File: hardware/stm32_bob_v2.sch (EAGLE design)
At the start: 54 parts, among them U1 F3_DISCOVERY, U2 LSF0108, U3 INA827, U4 INA827

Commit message: Added version 2 of board using 40 pin header
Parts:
- removed 5V_IO: (no value), SparkFun-Connectors:M081X08
- removed AIN1, AIN2, EXT_REF: M02PTH, SparkFun-Connectors:M02PTH
- removed JP1, JP2: M25X2, SparkFun-Connectors:M25X2
- added U$1: M40, SparkFun-Connectors:M40
- R10, R11, R12, R13, R6, R7, R8, R9: value (none) -> 1k
- R14, R15, R16, R17, R18, R19, R20, R21: value (none) -> 1.6k
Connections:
- removed net N$1: 5V_IO.1, R14.1, U2.B1
- removed net N$10: AIN1.2, U3.IN+
- removed net N$11: AIN2.2, U4.IN+
- removed net N$12: AIN2.1, U4.IN-
- removed net N$2: 5V_IO.2, R15.1, U2.B2
- removed net N$3: 5V_IO.3, R16.1, U2.B3
- removed net N$4: 5V_IO.4, R17.1, U2.B4
- removed net N$5: 5V_IO.5, R18.2, U2.B5
- removed net N$6: 5V_IO.6, R19.2, U2.B6
- removed net N$7: 5V_IO.7, R20.2, U2.B7
- removed net N$8: 5V_IO.8, R21.2, U2.B8
- removed net N$9: AIN1.1, U3.IN-
- new net AIN1_N: U$1.35, U3.IN-
- new net AIN1_P: U$1.36, U3.IN+
- new net AIN2_N: U$1.37, U4.IN-
- new net AIN2_P: U$1.38, U4.IN+
- new net PA14_5: R18.2, U$1.29, U2.B5
- new net PA15_5: R19.2, U$1.28, U2.B6
- new net PC10_5: R20.2, U$1.27, U2.B7
- new net PC11_5: R21.2, U$1.26, U2.B8
- new net PE11_5: R15.1, U$1.33, U2.B2
- new net PE13_5: R16.1, U$1.32, U2.B3
- new net PE14_5: R17.1, U$1.31, U2.B4
- new net PE9_5: R14.1, U$1.34, U2.B1
- net 3V: now also C1.1, C2.1, U$1.1, U$1.2, U3.V+, U4.V+; no longer JP1.1, JP1.2
- net 5V: now also U$1.3, U$1.4; no longer C1.1, C2.1, JP2.1, JP2.2, U3.V+, U4.V+
- net BOOT0: no longer JP2.19
- net GND: now also U$1.10, U$1.20, U$1.30, U$1.40; no longer EXT_REF.1, JP1.3, JP1.49, JP1.50, JP2.49, JP2.50
- net NRST: no longer JP1.4
- net PA0: no longer JP1.12
- net PA1: now also U$1.5; no longer JP1.9
- net PA10: no longer JP2.43
- net PA11: now also U$1.21; no longer JP2.42
- net PA12: now also U$1.22; no longer JP2.41
- net PA13: no longer JP2.40
- net PA14: no longer JP2.37
- net PA15: no longer JP2.38
- net PA2: now also U$1.6; no longer JP1.14
- net PA3: now also U$1.7; no longer JP1.11
- net PA4: no longer JP1.16
- net PA5: now also U$1.9; no longer JP1.15
- net PA6: now also U$1.11; no longer JP1.18
- net PA7: now also U$1.12; no longer JP1.17
- net PA8: no longer JP2.45
- net PA9: no longer JP2.44
- net PB0: no longer JP1.22
- net PB1: now also U$1.23; no longer JP1.21
- net PB10: no longer JP1.34
- net PB11: no longer JP1.33
- net PB12: now also U$1.25; no longer JP1.36
- net PB13: no longer JP1.35
- net PB14: no longer JP1.38
- net PB15: no longer JP1.37
- net PB2: no longer JP1.24
- net PB3: now also U$1.17; no longer JP2.26
- net PB4: now also U$1.18; no longer JP2.23
- net PB5: now also U$1.19; no longer JP2.24
- net PB6: no longer JP2.21
- net PB7: no longer JP2.22
- net PB8: no longer JP2.17
- net PB9: no longer JP2.18
- net PC0: no longer JP1.6
- net PC1: no longer JP1.5
- net PC10: no longer JP2.35
- net PC11: no longer JP2.36
- net PC12: no longer JP2.33
- net PC13: no longer JP2.10
- net PC14: no longer JP2.7
- net PC15: no longer JP2.8
- net PC2: no longer JP1.8
- net PC3: no longer JP1.7
- net PC4: no longer JP1.20
- net PC5: no longer JP1.19
- net PC6: now also U$1.13; no longer JP1.47
- net PC7: now also U$1.14; no longer JP1.48
- net PC8: now also U$1.15; no longer JP2.47
- net PC9: now also U$1.16; no longer JP2.46
- net PD0: no longer JP2.34
- net PD1: no longer JP2.31
- net PD10: no longer JP1.42
- net PD11: no longer JP1.41
- net PD12: no longer JP1.44
- net PD13: no longer JP1.43
- net PD14: no longer JP1.46
- net PD15: no longer JP1.45
- net PD2: no longer JP2.32
- net PD3: no longer JP2.29
- net PD4: no longer JP2.30
- net PD5: no longer JP2.27
- net PD6: no longer JP2.28
- net PD7: no longer JP2.25
- net PD8: no longer JP1.40
- net PD9: no longer JP1.39
- net PE0: no longer JP2.15
- net PE1: no longer JP2.16
- net PE10: no longer JP1.28
- net PE11: no longer JP1.27
- net PE12: no longer JP1.30
- net PE13: no longer JP1.29
- net PE14: no longer JP1.32
- net PE15: now also U$1.24; no longer JP1.31
- net PE2: no longer JP2.13
- net PE3: no longer JP2.14
- net PE4: no longer JP2.11
- net PE5: no longer JP2.12
- net PE6: no longer JP2.9
- net PE7: no longer JP1.23
- net PE8: no longer JP1.26
- net PE9: no longer JP1.25
- net PF0: no longer JP2.5
- net PF1: no longer JP2.6
- net PF10: no longer JP2.4
- net PF2: no longer JP1.10
- net PF4: now also U$1.8; no longer JP1.13
- net PF6: no longer JP2.39
- net PF9: no longer JP2.3
- net REF_EXT: now also U$1.39; no longer EXT_REF.2
- net VDD: no longer JP2.20

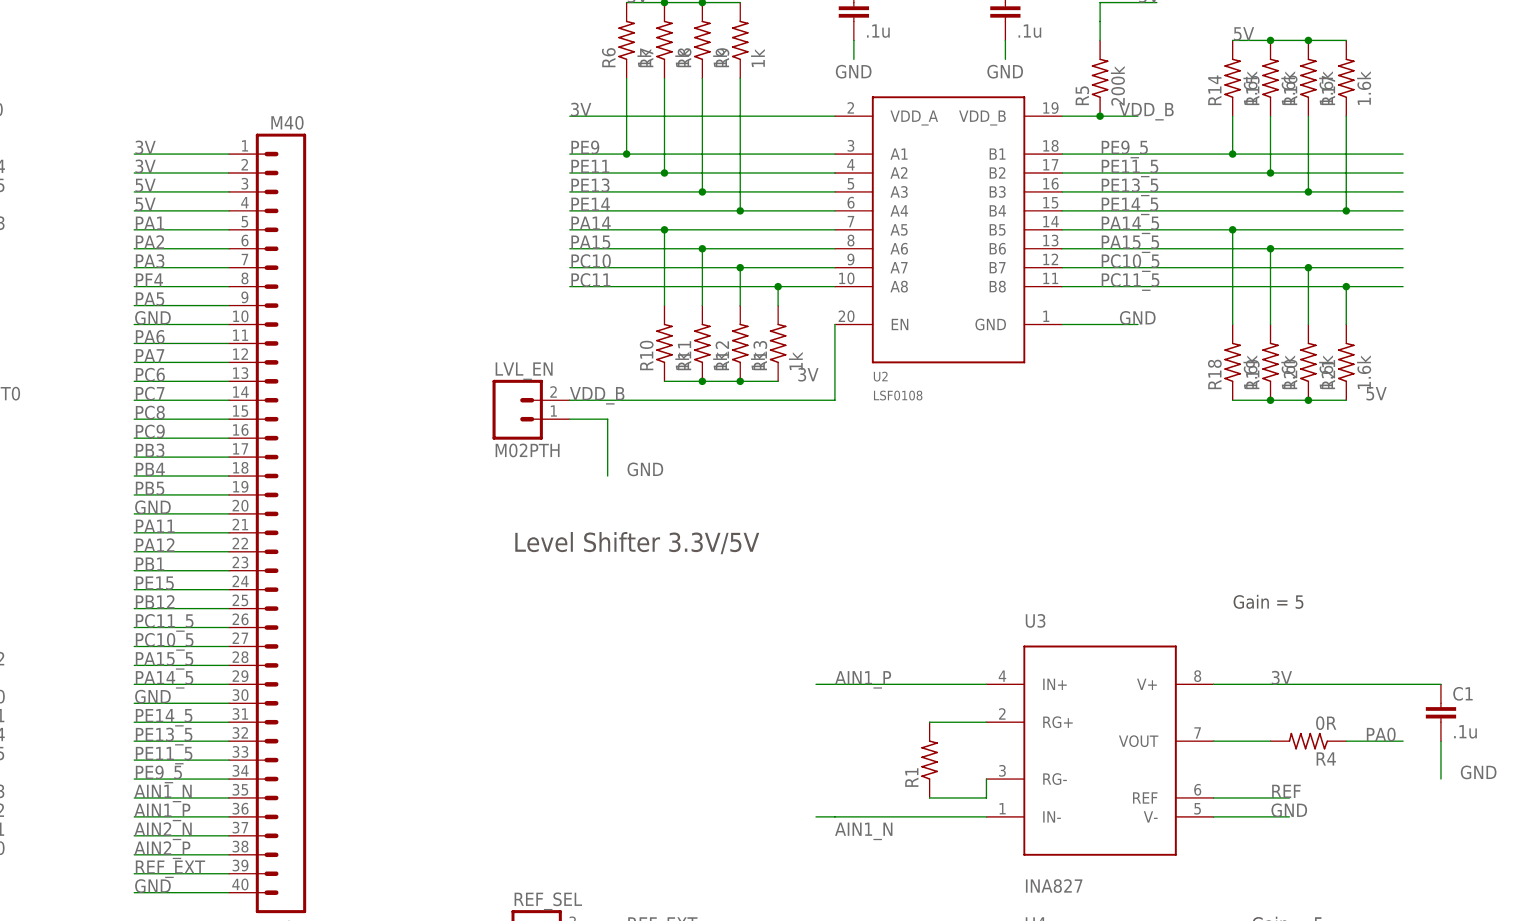
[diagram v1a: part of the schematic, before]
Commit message: changed io to avoid pins used on development board
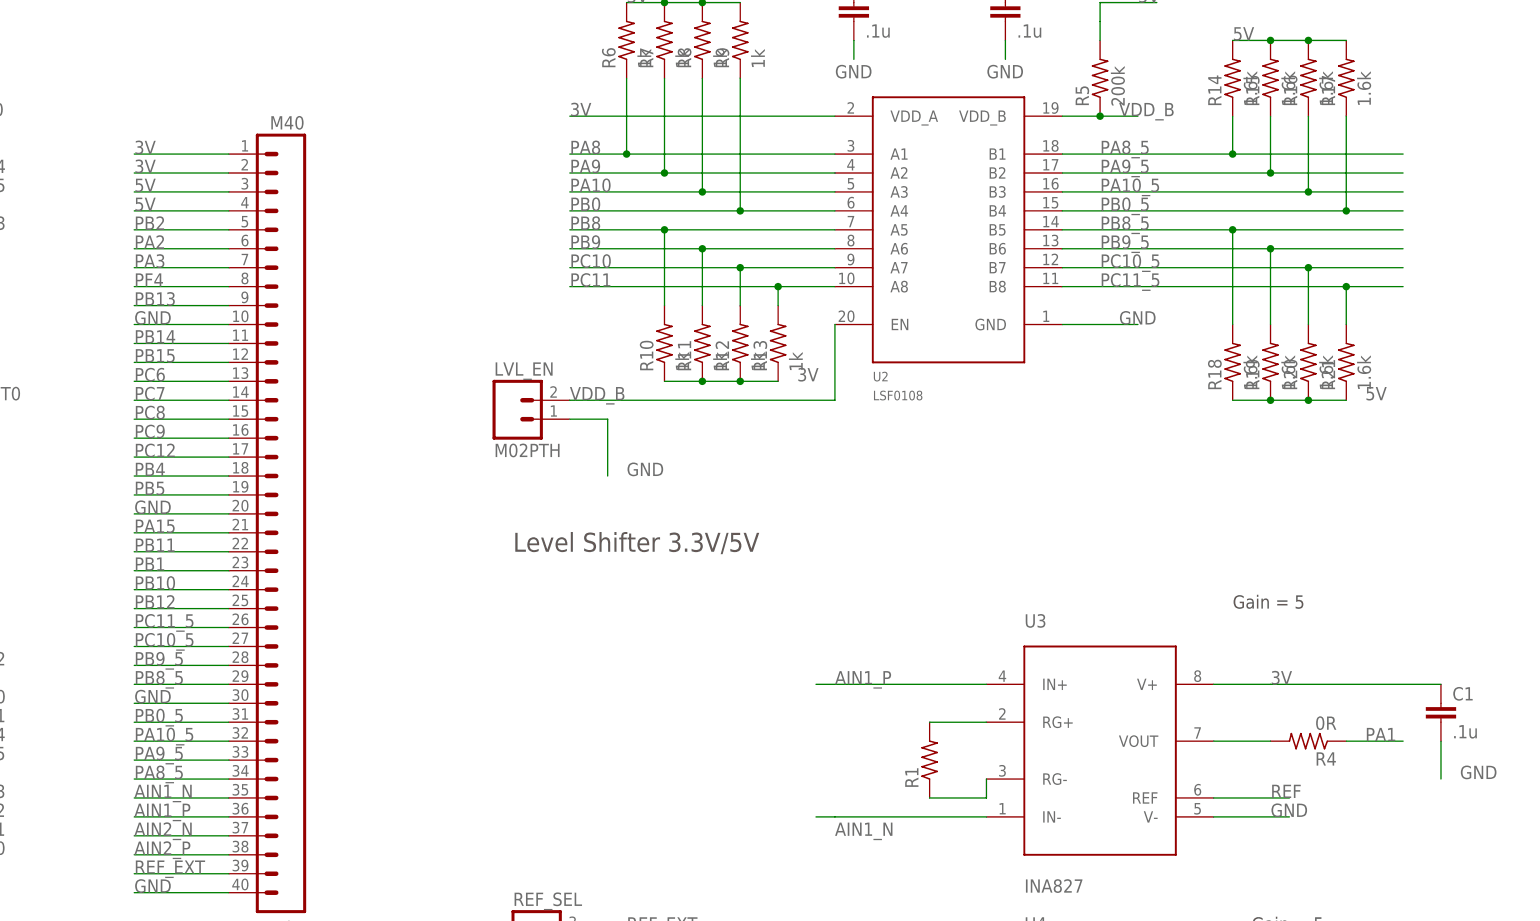
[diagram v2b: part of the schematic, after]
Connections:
- net PA14_5 renamed PB8_5
- net PA15_5 renamed PB9_5
- net PE11_5 renamed PA9_5
- net PE13_5 renamed PA10_5
- net PE14_5 renamed PB0_5
- net PE9_5 renamed PA8_5
- net PA0: no longer R4.1
- net PA1: now also R4.1; no longer U$1.5
- net PA10: now also R8.1, U2.A3
- net PA11: no longer U$1.21
- net PA12: no longer U$1.22
- net PA14: no longer R10.2, U2.A5
- net PA15: now also U$1.21; no longer R11.2, U2.A6
- net PA5: no longer U$1.9
- net PA6: no longer U$1.11
- net PA7: no longer U$1.12
- net PA8: now also R6.1, U2.A1
- net PA9: now also R7.1, U2.A2
- net PB0: now also R9.1, U2.A4
- net PB10: now also U$1.24
- net PB11: now also U$1.22
- net PB13: now also U$1.9
- net PB14: now also U$1.11
- net PB15: now also U$1.12
- net PB2: now also U$1.5
- net PB3: no longer U$1.17
- net PB8: now also R10.2, U2.A5
- net PB9: now also R11.2, U2.A6
- net PC12: now also U$1.17
- net PE11: no longer R7.1, U2.A2
- net PE13: no longer R8.1, U2.A3
- net PE14: no longer R9.1, U2.A4
- net PE15: no longer U$1.24
- net PE9: no longer R6.1, U2.A1
